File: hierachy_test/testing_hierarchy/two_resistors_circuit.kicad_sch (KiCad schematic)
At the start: 2 parts

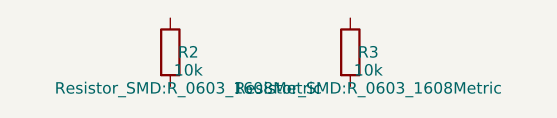
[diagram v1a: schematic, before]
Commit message: generating hierarchies, but not parts now
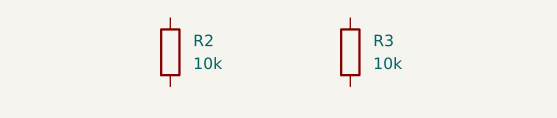
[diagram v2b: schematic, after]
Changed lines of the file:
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@@
     (dnp no)
     (fields_autoplaced yes)
-    (property "Reference" "R2" (at 2.00 0.00 0))
-    (property "Value" "10k" (at 2.00 2.00 0))
-    (property "Footprint" "Resistor_SMD:R_0603_1608Metric" (at 2.00 4.00 0))
+    (property "Reference" "R2"
+      (at 2.54 -1.27 0)
+      (effects
+        (font
+          (size 1.27 1.27)
+        )
+        (justify left)
+      )
+    )
+    (property "Value" "10k"
+      (at 2.54 1.27 0)
+      (effects
+        (font
+          (size 1.27 1.27)
+        )
+        (justify left)
+      )
+    )
+    (property "Footprint" "Resistor_SMD:R_0603_1608Metric"
+      (at -1.78 0.00 90)
+      (effects
+        (font
+          (size 1.27 1.27)
+        )
+        (hide yes)
+      )
+    )
+    (property "Datasheet" "~"
+      (at 0.00 0.00 0)
+      (effects
+        (font
+          (size 1.27 1.27)
+        )
+        (hide yes)
+      )
+    )
+    (property "Description" "Resistor"
+      (at 0.00 0.00 0)
+      (effects
+        (font
+          (size 1.27 1.27)
+        )
+        (hide yes)
+      )
+    )
+    (pin "2"
+    )
+    (pin "1"
+    )
+    (instances
+      (project "testing_hierarchy"
+        (path "/"
+          (reference "R2")
+          (unit 1)
+        )
+      )
+    )
   )
   (symbol
@@
     (dnp no)
     (fields_autoplaced yes)
-    (property "Reference" "R3" (at 22.00 0.00 0))
-    (property "Value" "10k" (at 22.00 2.00 0))
-    (property "Footprint" "Resistor_SMD:R_0603_1608Metric" (at 22.00 4.00 0))
+    (property "Reference" "R3"
+      (at 22.54 -1.27 0)
+      (effects
+        (font
+          (size 1.27 1.27)
+        )
+        (justify left)
+      )
+    )
+    (property "Value" "10k"
+      (at 22.54 1.27 0)
+      (effects
+        (font
+          (size 1.27 1.27)
+        )
+        (justify left)
+      )
+    )
+    (property "Footprint" "Resistor_SMD:R_0603_1608Metric"
+      (at 18.22 0.00 90)
+      (effects
+        (font
+          (size 1.27 1.27)
+        )
+        (hide yes)
+      )
+    )
+    (property "Datasheet" "~"
+      (at 20.00 0.00 0)
+      (effects
+        (font
+          (size 1.27 1.27)
+        )
+        (hide yes)
+      )
+    )
+    (property "Description" "Resistor"
+      (at 20.00 0.00 0)
+      (effects
+        (font
+          (size 1.27 1.27)
+        )
+        (hide yes)
+      )
+    )
+    (pin "2"
+    )
+    (pin "1"
+    )
+    (instances
+      (project "testing_hierarchy"
+        (path "/"
+          (reference "R3")
+          (unit 1)
+        )
+      )
+    )
   )
   (sheet_instances
